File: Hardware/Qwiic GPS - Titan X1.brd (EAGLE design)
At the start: 30.5 x 25.4 mm, 37 parts, among them J1 U.FL, J2 Qwiic Right Angle, J3 PTH, J4 Qwiic Right Angle, U1 Titan X1 GPS

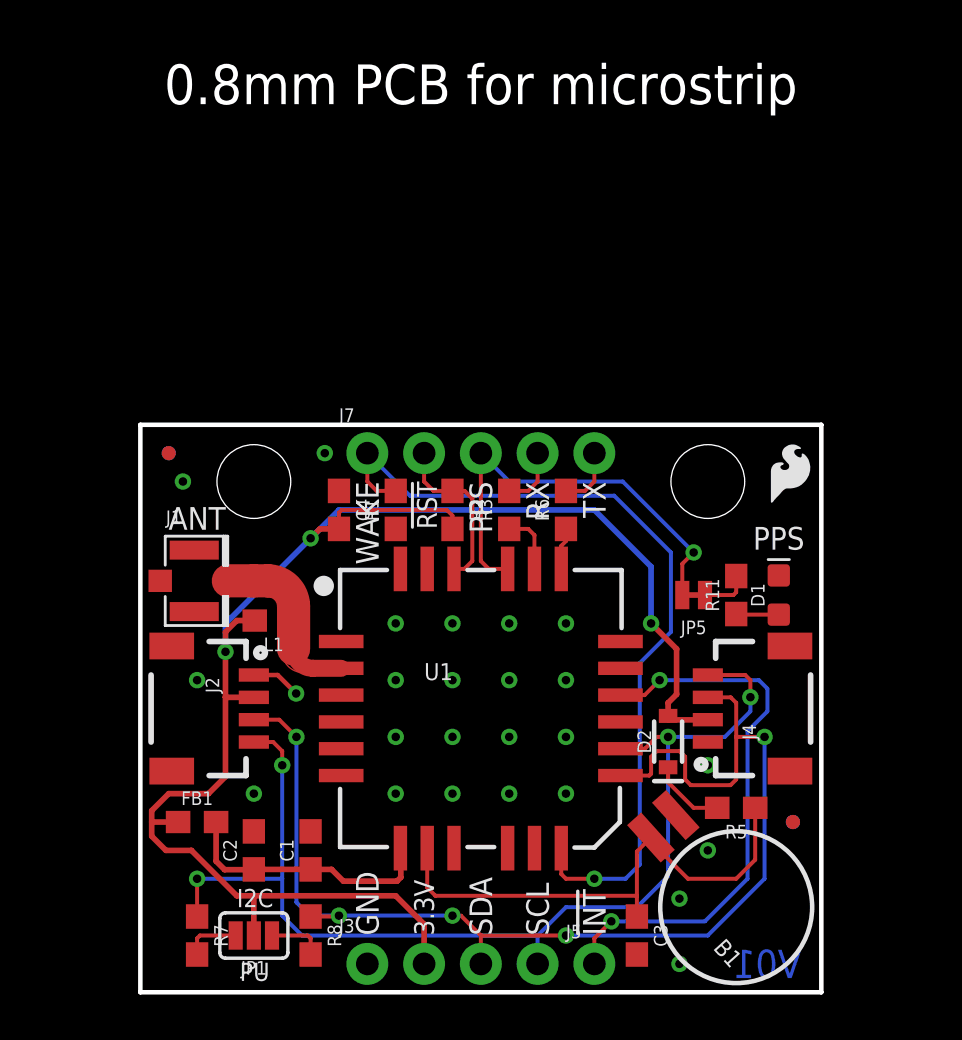
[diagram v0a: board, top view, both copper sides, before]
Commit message: V02 changed some net issues, board thicknessinstruction
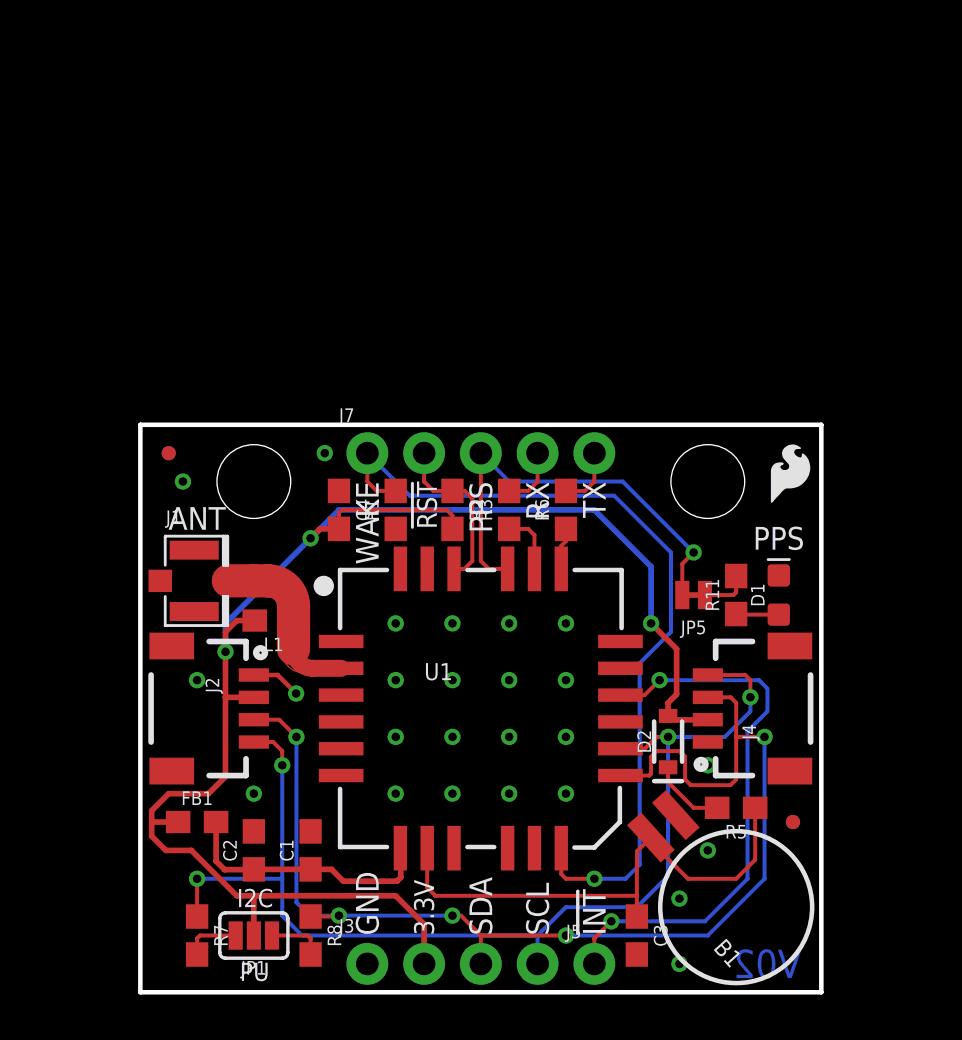
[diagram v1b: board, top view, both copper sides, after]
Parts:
- added U$3: SPECIAL_INSTRUCTIONS-PRODUCTION, SparkFun-Aesthetics:PRODUCTION_INSTRUCTIONS
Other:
- board text added: "V02"
- board text removed: "V01"
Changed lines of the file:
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@@
 <text x="20.32" y="2.54" size="1.016" layer="22" font="vector" ratio="15" rot="MR90" align="center-left">!INT</text>
 <text x="10.16" y="2.54" size="1.016" layer="22" font="vector" ratio="15" rot="MR90" align="center-left">GND</text>
-<text x="28.067" y="1.27" size="1.27" layer="16" font="vector" ratio="15" rot="MR180" align="center">V01</text>
+<text x="28.067" y="1.27" size="1.27" layer="16" font="vector" ratio="15" rot="MR180" align="center">V02</text>
 <text x="15.24" y="22.86" size="1.016" layer="21" font="vector" ratio="15" rot="R270" align="center-left">PPS</text>
 <text x="17.78" y="22.86" size="1.016" layer="21" font="vector" ratio="15" rot="R270" align="center-left">RX</text>
@@
 <text x="2.54" y="21.209" size="1.016" layer="21" font="vector" ratio="15" rot="R180" align="center">ANT</text>
 <text x="28.575" y="20.32" size="1.016" layer="21" font="vector" ratio="15" rot="R180" align="center">PPS</text>
-<text x="15.24" y="40.64" size="1.778" layer="20" font="vector" ratio="15" align="center">0.8mm PCB for microstrip</text>
+<text x="-15.24" y="-33.02" size="1.778" layer="51" font="vector" ratio="15" align="center">0.8mm PCB for microstrip</text>
 <text x="15.24" y="13.97" size="1.778" layer="22" font="vector" ratio="15" rot="SMR0" align="center">Qwiic
 GPS</text>
@@
 <element name="JP8" library="SparkFun" package="MICRO-FIDUCIAL" value="FIDUCIALUFIDUCIAL" x="1.27" y="24.13" rot="MR0"/>
 <element name="U$2" library="SparkFun-Aesthetics" package="SFE_LOGO_FLAME_.1" value="" x="27.94" y="21.59"/>
+<element name="U$3" library="SparkFun-Aesthetics" package="PRODUCTION_INSTRUCTIONS" value="SPECIAL_INSTRUCTIONS-PRODUCTION" x="-35.56" y="-21.59"/>
 </elements>
 <signals>
